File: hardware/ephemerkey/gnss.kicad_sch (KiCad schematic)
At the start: 12 parts

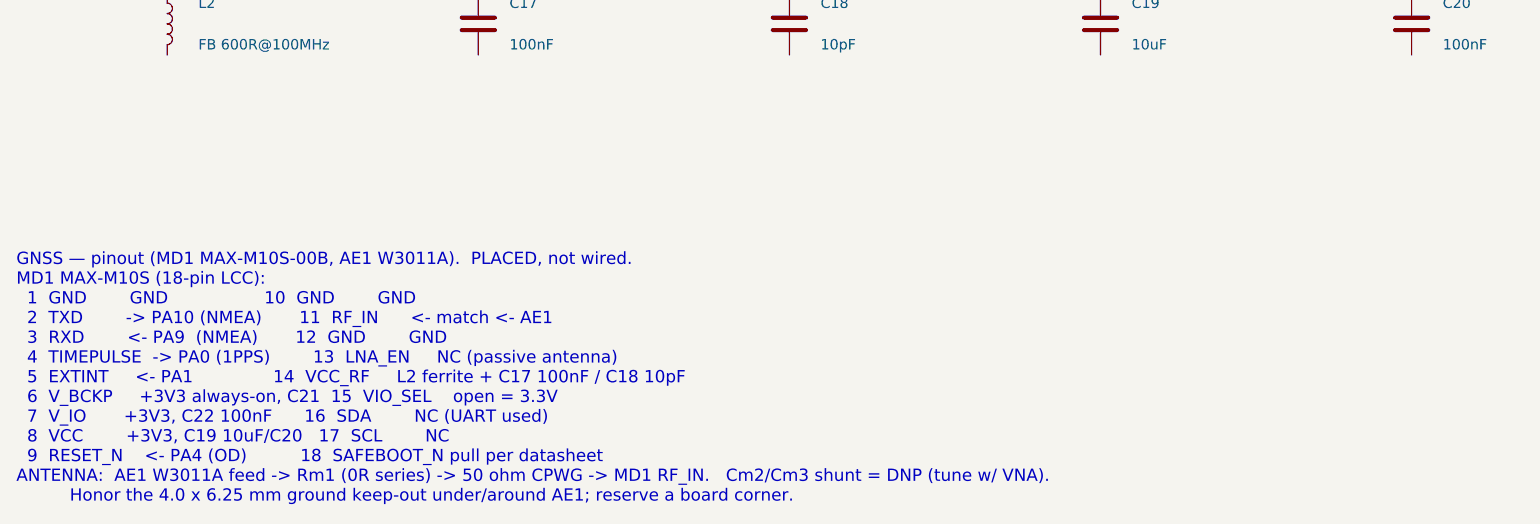
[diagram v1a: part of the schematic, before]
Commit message: lock: second servo output, clearer wiring notes, start PCB layout
- Add a second servo output (J8 + SERVO_SIG2 on PB4, R24/R25) sharing the
  VSERVO rail and the load-switch/interlock -- e.g. a dual-latch lock.
- Rewrite the per-sheet wiring notes (MCU/PWR/DRV) from prose into terse
  pin -> net maps: one line per part, every pin = its net, with a NETS IN
  header for cross-sheet signals. Rationale stays in the README.
- kschgen: park the wiring note below all placed components so the text no
  longer overlaps symbols (computed from the last component row).
- Start the lock PCB layout (hardware/lock/lock.kicad_pcb).

Board regenerates + checks clean (49 components; all footprints carry 3D models).

Co-Authored-By: Claude Opus 4.8 (1M context) <noreply@anthropic.com>
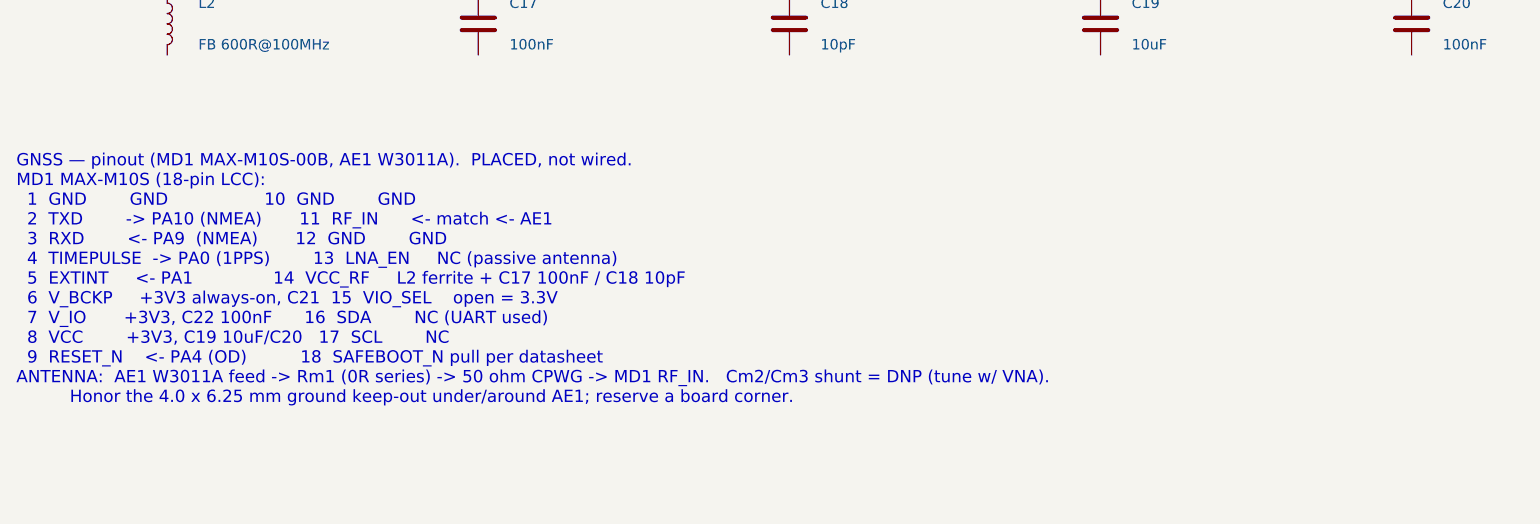
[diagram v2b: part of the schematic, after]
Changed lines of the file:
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@@
 		(instances
 			(project "ephemerkey"
-				(path "/e1000000-0000-4000-8000-000000000001/ef82131c-a395-487c-95e1-ff0b4d3a449c"
+				(path "/e1000000-0000-4000-8000-000000000001/25566662-6e3a-4f50-95ef-bf4b942efb81"
 					(reference "MD1")
 					(unit 1)
@@
 		(instances
 			(project "ephemerkey"
-				(path "/e1000000-0000-4000-8000-000000000001/ef82131c-a395-487c-95e1-ff0b4d3a449c"
+				(path "/e1000000-0000-4000-8000-000000000001/25566662-6e3a-4f50-95ef-bf4b942efb81"
 					(reference "AE1")
 					(unit 1)
@@
 		(instances
 			(project "ephemerkey"
-				(path "/e1000000-0000-4000-8000-000000000001/ef82131c-a395-487c-95e1-ff0b4d3a449c"
+				(path "/e1000000-0000-4000-8000-000000000001/25566662-6e3a-4f50-95ef-bf4b942efb81"
 					(reference "L2")
 					(unit 1)
@@
 		(instances
 			(project "ephemerkey"
-				(path "/e1000000-0000-4000-8000-000000000001/ef82131c-a395-487c-95e1-ff0b4d3a449c"
+				(path "/e1000000-0000-4000-8000-000000000001/25566662-6e3a-4f50-95ef-bf4b942efb81"
 					(reference "C17")
 					(unit 1)
@@
 		(instances
 			(project "ephemerkey"
-				(path "/e1000000-0000-4000-8000-000000000001/ef82131c-a395-487c-95e1-ff0b4d3a449c"
+				(path "/e1000000-0000-4000-8000-000000000001/25566662-6e3a-4f50-95ef-bf4b942efb81"
 					(reference "C18")
 					(unit 1)
@@
 		(instances
 			(project "ephemerkey"
-				(path "/e1000000-0000-4000-8000-000000000001/ef82131c-a395-487c-95e1-ff0b4d3a449c"
+				(path "/e1000000-0000-4000-8000-000000000001/25566662-6e3a-4f50-95ef-bf4b942efb81"
 					(reference "C19")
 					(unit 1)
@@
 		(instances
 			(project "ephemerkey"
-				(path "/e1000000-0000-4000-8000-000000000001/ef82131c-a395-487c-95e1-ff0b4d3a449c"
+				(path "/e1000000-0000-4000-8000-000000000001/25566662-6e3a-4f50-95ef-bf4b942efb81"
 					(reference "C20")
 					(unit 1)
@@
 		(instances
 			(project "ephemerkey"
-				(path "/e1000000-0000-4000-8000-000000000001/ef82131c-a395-487c-95e1-ff0b4d3a449c"
+				(path "/e1000000-0000-4000-8000-000000000001/25566662-6e3a-4f50-95ef-bf4b942efb81"
 					(reference "C21")
 					(unit 1)
@@
 		(instances
 			(project "ephemerkey"
-				(path "/e1000000-0000-4000-8000-000000000001/ef82131c-a395-487c-95e1-ff0b4d3a449c"
+				(path "/e1000000-0000-4000-8000-000000000001/25566662-6e3a-4f50-95ef-bf4b942efb81"
 					(reference "C22")
 					(unit 1)
@@
 		(instances
 			(project "ephemerkey"
-				(path "/e1000000-0000-4000-8000-000000000001/ef82131c-a395-487c-95e1-ff0b4d3a449c"
+				(path "/e1000000-0000-4000-8000-000000000001/25566662-6e3a-4f50-95ef-bf4b942efb81"
 					(reference "Rm1")
 					(unit 1)
@@
 		(instances
 			(project "ephemerkey"
-				(path "/e1000000-0000-4000-8000-000000000001/ef82131c-a395-487c-95e1-ff0b4d3a449c"
+				(path "/e1000000-0000-4000-8000-000000000001/25566662-6e3a-4f50-95ef-bf4b942efb81"
 					(reference "Cm2")
 					(unit 1)
@@
 		(instances
 			(project "ephemerkey"
-				(path "/e1000000-0000-4000-8000-000000000001/ef82131c-a395-487c-95e1-ff0b4d3a449c"
+				(path "/e1000000-0000-4000-8000-000000000001/25566662-6e3a-4f50-95ef-bf4b942efb81"
 					(reference "Cm3")
 					(unit 1)
@@
 	(text "GNSS — pinout (MD1 MAX-M10S-00B, AE1 W3011A).  PLACED, not wired.\nMD1 MAX-M10S (18-pin LCC):\n  1  GND        GND                  10  GND        GND\n  2  TXD        -> PA10 (NMEA)       11  RF_IN      <- match <- AE1\n  3  RXD        <- PA9  (NMEA)       12  GND        GND\n  4  TIMEPULSE  -> PA0 (1PPS)        13  LNA_EN     NC (passive antenna)\n  5  EXTINT     <- PA1               14  VCC_RF     L2 ferrite + C17 100nF / C18 10pF\n  6  V_BCKP     +3V3 always-on, C21  15  VIO_SEL    open = 3.3V\n  7  V_IO       +3V3, C22 100nF      16  SDA        NC (UART used)\n  8  VCC        +3V3, C19 10uF/C20   17  SCL        NC\n  9  RESET_N    <- PA4 (OD)          18  SAFEBOOT_N pull per datasheet\nANTENNA:  AE1 W3011A feed -> Rm1 (0R series) -> 50 ohm CPWG -> MD1 RF_IN.   Cm2/Cm3 shunt = DNP (tune w/ VNA).\n          Honor the 4.0 x 6.25 mm ground keep-out under/around AE1; reserve a board corner."
 		(exclude_from_sim no)
-		(at 12.00 150.00 0)
+		(at 12.00 137.92 0)
 		(effects (font (size 1.5 1.5)) (justify left top))
 	)

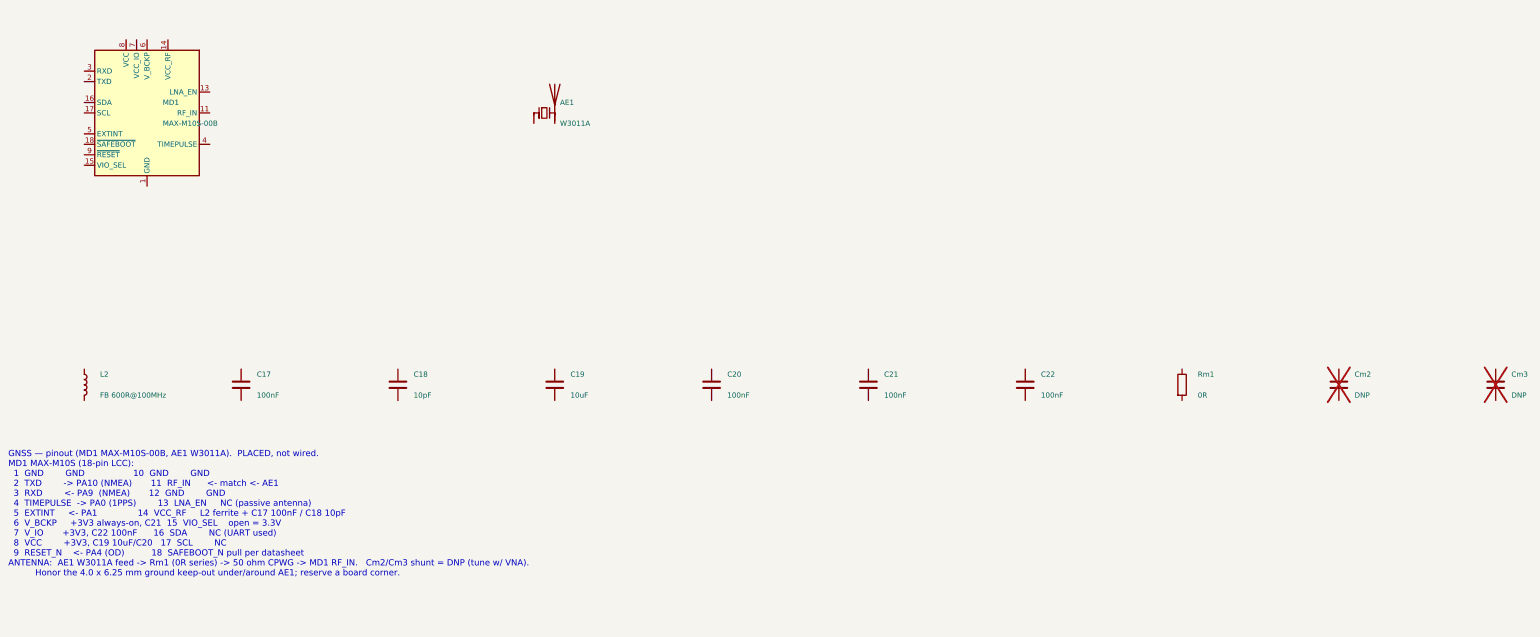
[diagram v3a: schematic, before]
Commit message: ephemerkey: add buzzer (PB4/TIM3_CH1), 2nd vertical USB-C, antenna 1.8pF shunt
- Beeper: LS1 MLT-8530 (C94599, 3.6V magnetic transducer) + AO3400A low-side
  driver (Q2) + 1N4148W flyback (D5) + gate 100R/100k, driven by PB4/TIM3_CH1.
  PB4 verified as TIM3_CH1 (AF1) on the U0 family AF map; TIM3 free (PPS uses TIM2).
  Buzzer footprint is the CUI CMT-8504 placeholder -- verify vs MLT-8530 at layout.
- 2nd USB-C: J5 GCT USB4085 (C7095263), vertical, same 16-pin USB2.0 family,
  same bus as J3 (parallel VBUS/D+/D-/GND) with its own CC pulldowns R15/R16.
- Antenna: populate Cm2 = 1.8pF shunt (W3011A datasheet reference value; the -A's
  rated -16dB is measured with shunt 1.8pF), Cm3 DNP; VNA-trim at bring-up.
  MAX-M10S RF_IN has internal DC block -> no external DC-block cap. Refs: Pulse
  W3011A datasheet + u-blox MAX-M10S integration manual UBX-20053088.

Regenerated (70 components, all footprints assigned + 3D models). DESIGN.md +
per-sheet notes updated. ephemerkey was placed-not-wired, so no wiring lost.

Co-Authored-By: Claude Opus 4.8 (1M context) <noreply@anthropic.com>
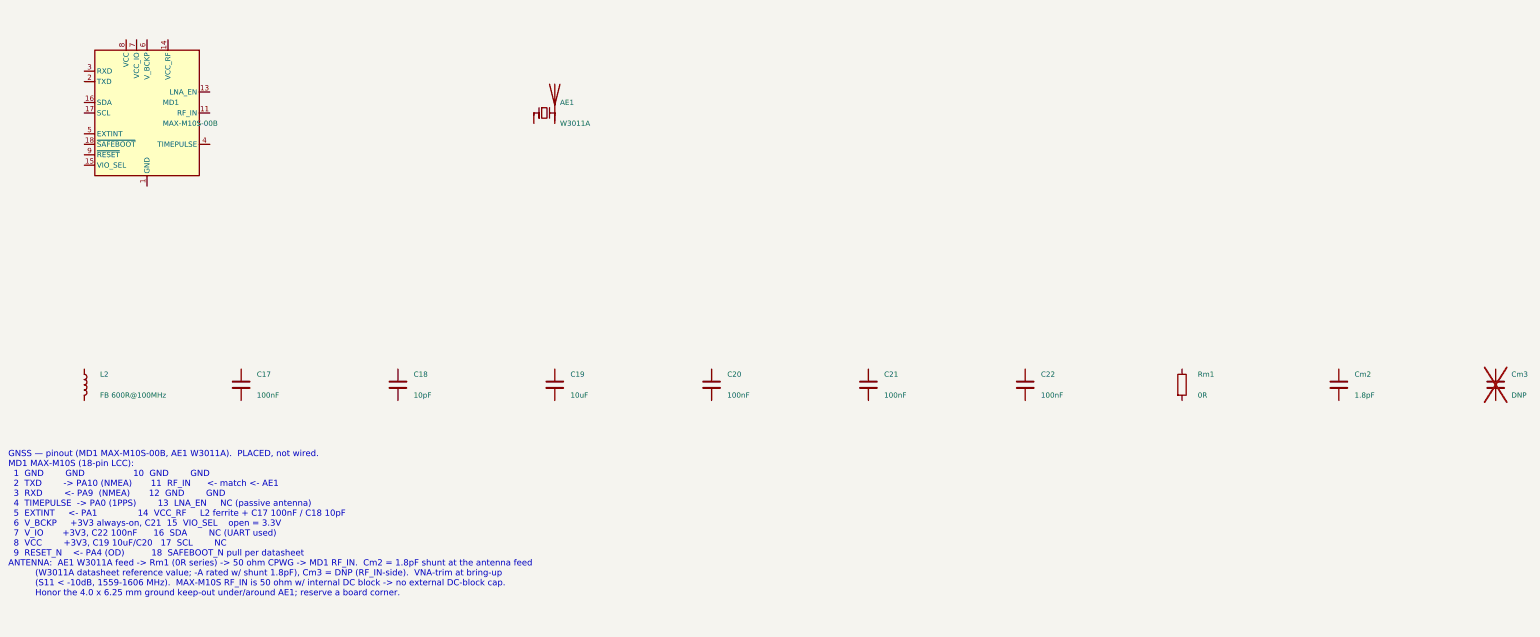
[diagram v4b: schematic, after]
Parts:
- Cm2: value DNP -> 1.8pF; LCSC (none) -> C1549; now fitted
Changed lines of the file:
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@@
 		(instances
 			(project "ephemerkey"
-				(path "/e1000000-0000-4000-8000-000000000001/fc1ebb90-de50-4d66-8e18-025b31174c33"
+				(path "/e1000000-0000-4000-8000-000000000001/b6d839e1-b7ff-4bba-963f-0862c69068ed"
 					(reference "MD1")
 					(unit 1)
@@
 		(instances
 			(project "ephemerkey"
-				(path "/e1000000-0000-4000-8000-000000000001/fc1ebb90-de50-4d66-8e18-025b31174c33"
+				(path "/e1000000-0000-4000-8000-000000000001/b6d839e1-b7ff-4bba-963f-0862c69068ed"
 					(reference "AE1")
 					(unit 1)
@@
 		(instances
 			(project "ephemerkey"
-				(path "/e1000000-0000-4000-8000-000000000001/fc1ebb90-de50-4d66-8e18-025b31174c33"
+				(path "/e1000000-0000-4000-8000-000000000001/b6d839e1-b7ff-4bba-963f-0862c69068ed"
 					(reference "L2")
 					(unit 1)
@@
 		(instances
 			(project "ephemerkey"
-				(path "/e1000000-0000-4000-8000-000000000001/fc1ebb90-de50-4d66-8e18-025b31174c33"
+				(path "/e1000000-0000-4000-8000-000000000001/b6d839e1-b7ff-4bba-963f-0862c69068ed"
 					(reference "C17")
 					(unit 1)
@@
 		(instances
 			(project "ephemerkey"
-				(path "/e1000000-0000-4000-8000-000000000001/fc1ebb90-de50-4d66-8e18-025b31174c33"
+				(path "/e1000000-0000-4000-8000-000000000001/b6d839e1-b7ff-4bba-963f-0862c69068ed"
 					(reference "C18")
 					(unit 1)
@@
 		(instances
 			(project "ephemerkey"
-				(path "/e1000000-0000-4000-8000-000000000001/fc1ebb90-de50-4d66-8e18-025b31174c33"
+				(path "/e1000000-0000-4000-8000-000000000001/b6d839e1-b7ff-4bba-963f-0862c69068ed"
 					(reference "C19")
 					(unit 1)
@@
 		(instances
 			(project "ephemerkey"
-				(path "/e1000000-0000-4000-8000-000000000001/fc1ebb90-de50-4d66-8e18-025b31174c33"
+				(path "/e1000000-0000-4000-8000-000000000001/b6d839e1-b7ff-4bba-963f-0862c69068ed"
 					(reference "C20")
 					(unit 1)
@@
 		(instances
 			(project "ephemerkey"
-				(path "/e1000000-0000-4000-8000-000000000001/fc1ebb90-de50-4d66-8e18-025b31174c33"
+				(path "/e1000000-0000-4000-8000-000000000001/b6d839e1-b7ff-4bba-963f-0862c69068ed"
 					(reference "C21")
 					(unit 1)
@@
 		(instances
 			(project "ephemerkey"
-				(path "/e1000000-0000-4000-8000-000000000001/fc1ebb90-de50-4d66-8e18-025b31174c33"
+				(path "/e1000000-0000-4000-8000-000000000001/b6d839e1-b7ff-4bba-963f-0862c69068ed"
 					(reference "C22")
 					(unit 1)
@@
 		(instances
 			(project "ephemerkey"
-				(path "/e1000000-0000-4000-8000-000000000001/fc1ebb90-de50-4d66-8e18-025b31174c33"
+				(path "/e1000000-0000-4000-8000-000000000001/b6d839e1-b7ff-4bba-963f-0862c69068ed"
 					(reference "Rm1")
 					(unit 1)
@@
 		(in_bom yes)
 		(on_board yes)
-		(dnp yes)
+		(dnp no)
 		(property "Reference" "Cm2"
 			(at 339.0900 119.3800 0)
 			(effects (font (size 1.27 1.27)) (justify left))
 		)
-		(property "Value" "DNP"
+		(property "Value" "1.8pF"
 			(at 339.0900 124.4600 0)
 			(effects (font (size 1.27 1.27)) (justify left))
@@
 			(effects (font (size 1.27 1.27))) (hide yes)
 		)
-		(pin "1")
-		(pin "2")
-		(instances
-			(project "ephemerkey"
-				(path "/e1000000-0000-4000-8000-000000000001/fc1ebb90-de50-4d66-8e18-025b31174c33"
+		(property "LCSC" "C1549"
+			(at 335.2800 121.9200 0)
+			(effects (font (size 1.27 1.27))) (hide yes)
+		)
+		(pin "1")
+		(pin "2")
+		(instances
+			(project "ephemerkey"
+				(path "/e1000000-0000-4000-8000-000000000001/b6d839e1-b7ff-4bba-963f-0862c69068ed"
 					(reference "Cm2")
 					(unit 1)
@@
 		(instances
 			(project "ephemerkey"
-				(path "/e1000000-0000-4000-8000-000000000001/fc1ebb90-de50-4d66-8e18-025b31174c33"
+				(path "/e1000000-0000-4000-8000-000000000001/b6d839e1-b7ff-4bba-963f-0862c69068ed"
 					(reference "Cm3")
 					(unit 1)
@@
 		)
 	)
-	(text "GNSS — pinout (MD1 MAX-M10S-00B, AE1 W3011A).  PLACED, not wired.\nMD1 MAX-M10S (18-pin LCC):\n  1  GND        GND                  10  GND        GND\n  2  TXD        -> PA10 (NMEA)       11  RF_IN      <- match <- AE1\n  3  RXD        <- PA9  (NMEA)       12  GND        GND\n  4  TIMEPULSE  -> PA0 (1PPS)        13  LNA_EN     NC (passive antenna)\n  5  EXTINT     <- PA1               14  VCC_RF     L2 ferrite + C17 100nF / C18 10pF\n  6  V_BCKP     +3V3 always-on, C21  15  VIO_SEL    open = 3.3V\n  7  V_IO       +3V3, C22 100nF      16  SDA        NC (UART used)\n  8  VCC        +3V3, C19 10uF/C20   17  SCL        NC\n  9  RESET_N    <- PA4 (OD)          18  SAFEBOOT_N pull per datasheet\nANTENNA:  AE1 W3011A feed -> Rm1 (0R series) -> 50 ohm CPWG -> MD1 RF_IN.   Cm2/Cm3 shunt = DNP (tune w/ VNA).\n          Honor the 4.0 x 6.25 mm ground keep-out under/around AE1; reserve a board corner."
+	(text "GNSS — pinout (MD1 MAX-M10S-00B, AE1 W3011A).  PLACED, not wired.\nMD1 MAX-M10S (18-pin LCC):\n  1  GND        GND                  10  GND        GND\n  2  TXD        -> PA10 (NMEA)       11  RF_IN      <- match <- AE1\n  3  RXD        <- PA9  (NMEA)       12  GND        GND\n  4  TIMEPULSE  -> PA0 (1PPS)        13  LNA_EN     NC (passive antenna)\n  5  EXTINT     <- PA1               14  VCC_RF     L2 ferrite + C17 100nF / C18 10pF\n  6  V_BCKP     +3V3 always-on, C21  15  VIO_SEL    open = 3.3V\n  7  V_IO       +3V3, C22 100nF      16  SDA        NC (UART used)\n  8  VCC        +3V3, C19 10uF/C20   17  SCL        NC\n  9  RESET_N    <- PA4 (OD)          18  SAFEBOOT_N pull per datasheet\nANTENNA:  AE1 W3011A feed -> Rm1 (0R series) -> 50 ohm CPWG -> MD1 RF_IN.  Cm2 = 1.8pF shunt at the antenna feed\n          (W3011A datasheet reference value; -A rated w/ shunt 1.8pF), Cm3 = DNP (RF_IN-side).  VNA-trim at bring-up\n          (S11 < -10dB, 1559-1606 MHz).  MAX-M10S RF_IN is 50 ohm w/ internal DC block -> no external DC-block cap.\n          Honor the 4.0 x 6.25 mm ground keep-out under/around AE1; reserve a board corner."
 		(exclude_from_sim no)
 		(at 12.00 137.92 0)
